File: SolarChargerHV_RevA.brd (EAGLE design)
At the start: 85 x 78 mm, 134 parts, among them CON1 CON_4X200MIL, CON2 USB_BMULTICOMP, CON3 ICSP, CON4 CON_3X100MIL, CON5 CON_3X100MIL, CON6 CON_8X200MIL, CON7 CON_2X100MIL, IC1 MCP3428, IC10 AT45DB161E, IC12 MCP14A0153, IC13 MCP14A0153, IC2 LMR62014, IC3 MIC4605-1YM, IC4 MCP1755, IC5 PIC18F46J50, IC6 TS6001, IC7 LMT86, IC8 24AA16, Q10 NTR4101PT1G, Q11 N-FET, Q12 N-FET, Q13 N-FET, Q14 N-FET, Q15 NX3008NBKW, Q2 PSMN6R0-30YL, Q3 NX3008NBKW, Q4 NTR4101PT1G, Q5 IPB039N10N3, Q6 IPB039N10N3, Q9 NX3008NBKW, X1 ABS07-120-32.768KHZ-T, X2 ABM3-8.000MHZ-D2Y-T, X3 USB_A, X4 USB_A

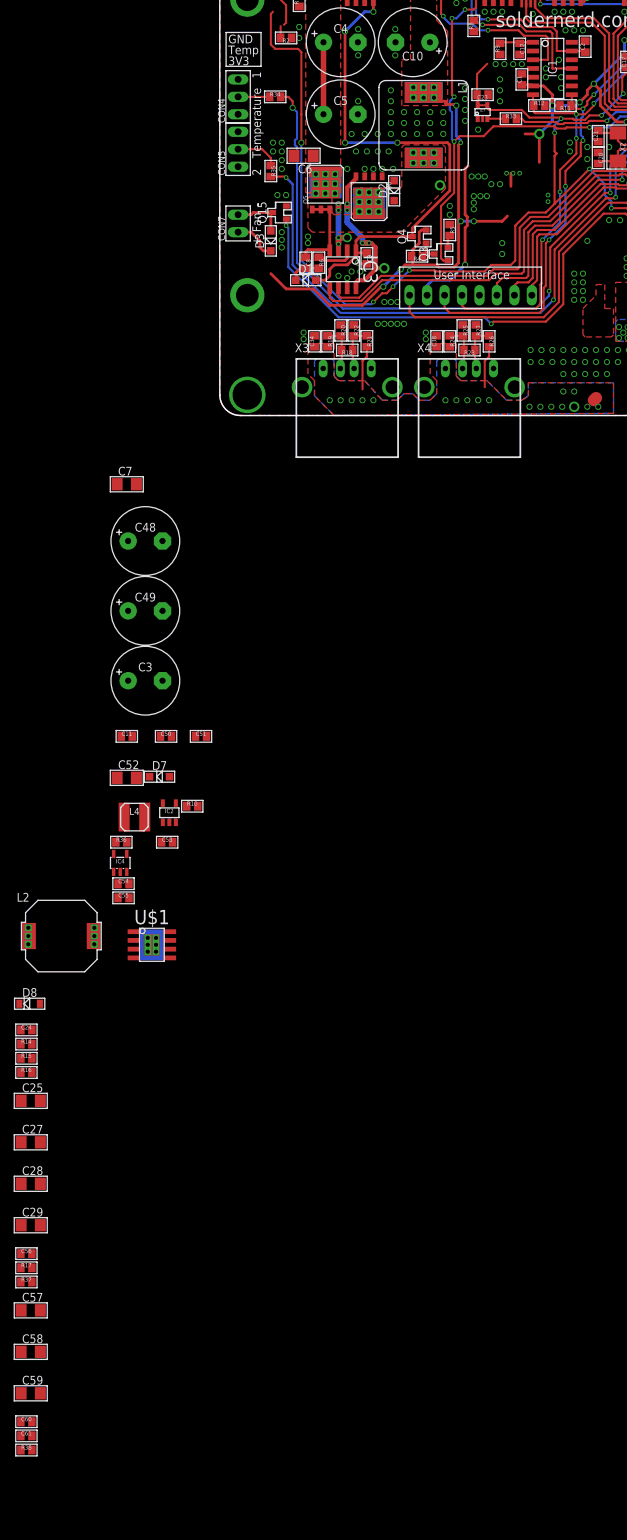
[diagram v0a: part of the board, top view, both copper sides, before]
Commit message: Buck for high voltage version nearly completed. Mosfet footprint still to be changed. Low-side current sensing implemented
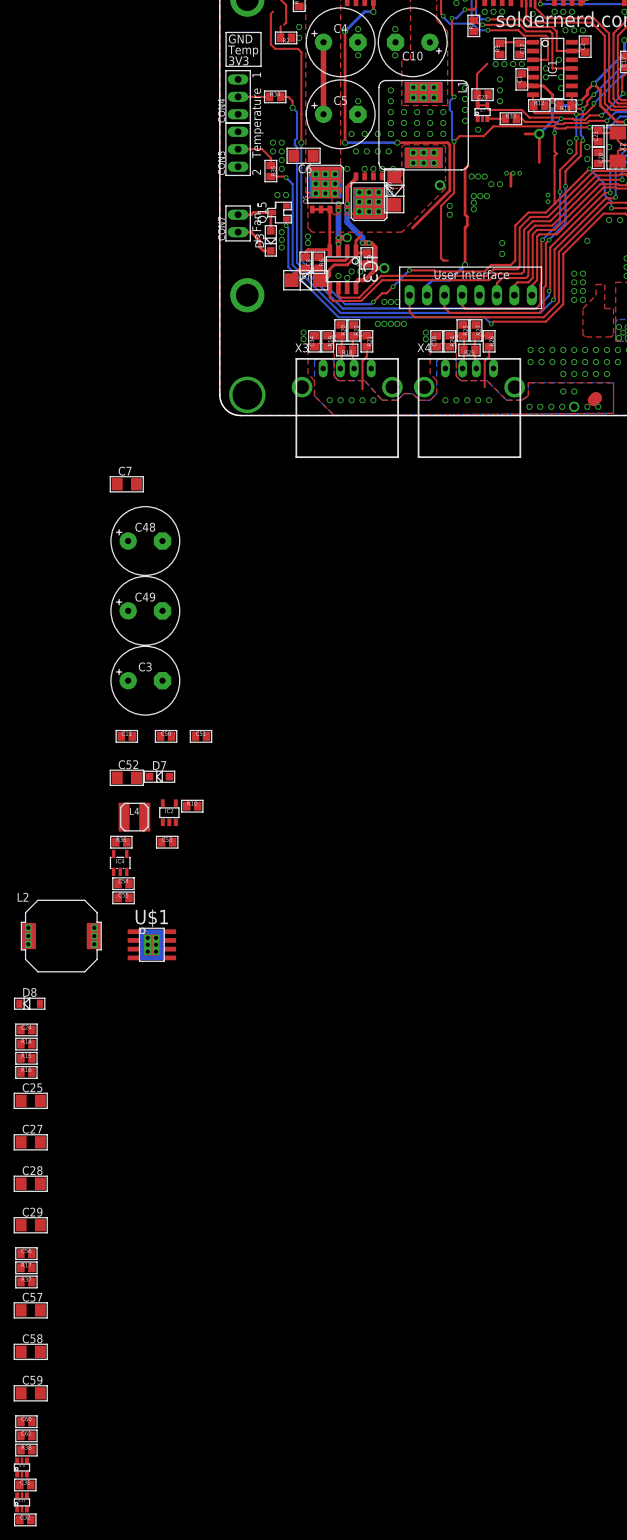
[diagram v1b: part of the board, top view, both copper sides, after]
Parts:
- removed Q3: NX3008NBKW, 00Mosfet:SOT23
- removed Q4: NTR4101PT1G, 00Mosfet:SOT23
- removed R4: 620k, 00Resistor:R0805
- removed R5: 300k, 00Resistor:R0805
- added C31, C32: 100n, 00Capacitor:C0805
- added IC11, IC9: INA213, 00Sensor:SC70-6
- D1, D2: value PMEG3010BER -> STPS2150; device 00Diode:SOD123 -> 00Diode:DO214AC
- D5: value 18V -> 70V
- D6: value 15V -> 48V
- Q2: value PSMN6R0-30YL -> IPB039N10N3
- R3, R7: value R003 -> R0025
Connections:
- removed net N$16: Q3.3, Q4.1, R4.1
- removed net N$19: Q3.2, R5.2
- removed net VIN_SENSE: C2.1, IC1.13, R1.1, R2.2
- removed net VOUT: C10.+, C3.+, L1.1, L1.1B, L1.1C, L1.1D, L1.1E, L1.1F, L1.1G, L1.1H, Q4.2, R4.2
- new net GNDINT: C10.-, C3.-, C4.-, C48.-, C49.-, C5.-, C6.2, C7.2, D2.A, IC11.5, IC9.4, Q6.1, Q6.2, Q6.3, R3.2, R7.1
- new net VIN_SENSE+: C2.2, IC1.13, R1.1, R2.2
- new net VIN_SENSE-: C2.1, IC1.14, IC9.5, Q2.1, Q2.2, Q2.3, R2.1, R3.1
- new net VOUT_SENSE+: C12.1, IC1.1
- net +3V3: now also C31.1, C32.1, IC11.3, IC9.3
- net BATTERY: now also C10.+, C3.+, L1.1, L1.1B, L1.1C, L1.1D, L1.1E, L1.1F, L1.1G, L1.1H
- net BUCK_ON: no longer Q3.1
- net BUCK_SUPPLY: no longer Q4.3
- net GND: now also C31.2, C32.2, IC11.1, IC11.2, IC11.4, IC9.1, IC9.2, R7.2; no longer C10.-, C2.2, C3.-, C4.-, C48.-, C49.-, C5.-, C6.2, C7.2, D2.A, D5.A, IC1.14, Q2.1, Q2.2, Q2.3, Q6.1, Q6.2, Q6.3, R2.1, R5.1
- net IIN_SENSE: now also IC9.6
- net IOUT_SENSE: now also IC11.6
- net PANEL-: now also D5.A
- net VOUT_SENSE: no longer C12.1, IC1.1
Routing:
- net VIN_SENSE: track 84.0 -> 0.00 mm, vias 2 -> 0
- net VIN_SENSE+: track 0.00 -> 83.8 mm, vias 0 -> 2
- net VOUT: track 72.2 -> 0.00 mm, vias 6 -> 0
- net BUCK_SUPPLY: track 74.1 -> 64.6 mm
- net N$16: track 3.43 -> 0.00 mm
- net VOUT_SENSE: track 5.49 -> 3.28 mm
- net N$19: track 1.85 -> 0.00 mm
- net VOUT_SENSE+: track 0.00 -> 1.78 mm
- net N$1: track 4.93 -> 5.52 mm

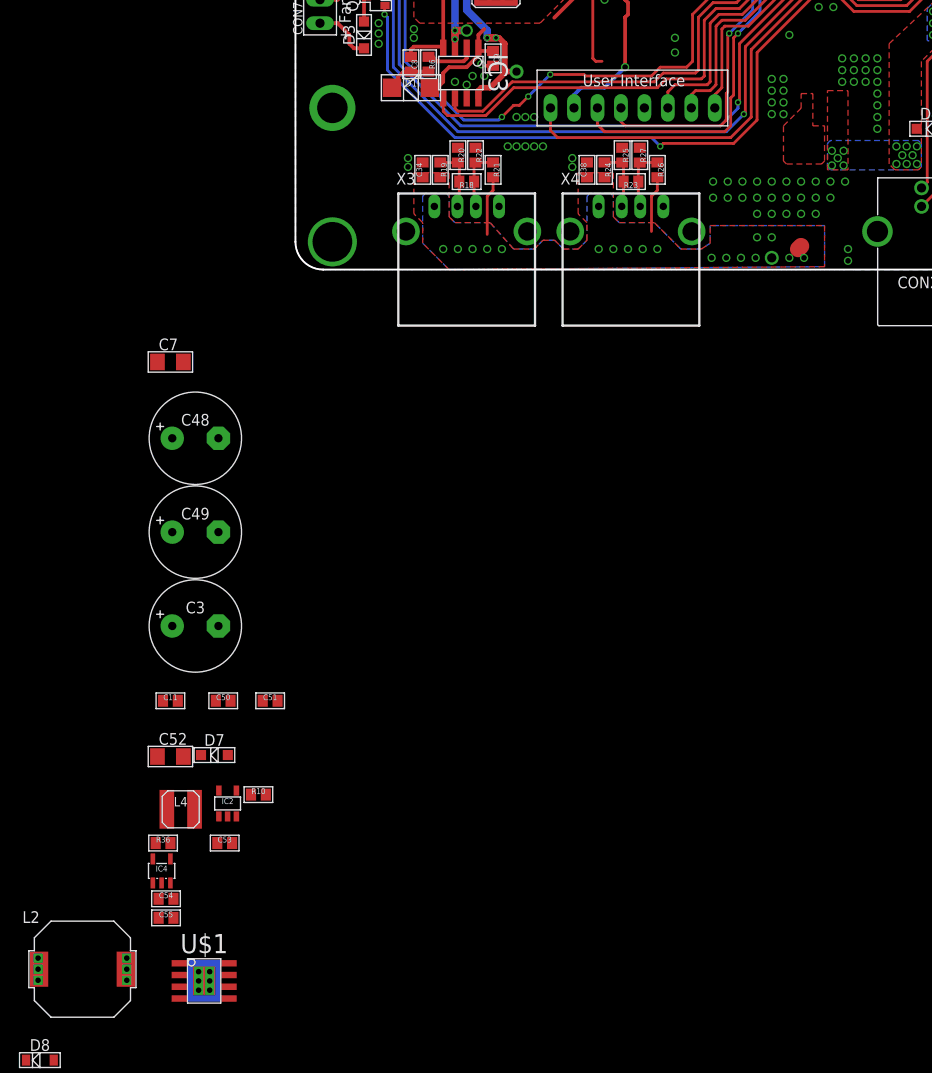
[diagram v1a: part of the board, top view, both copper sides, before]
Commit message: Flash now supplied directly from VCC
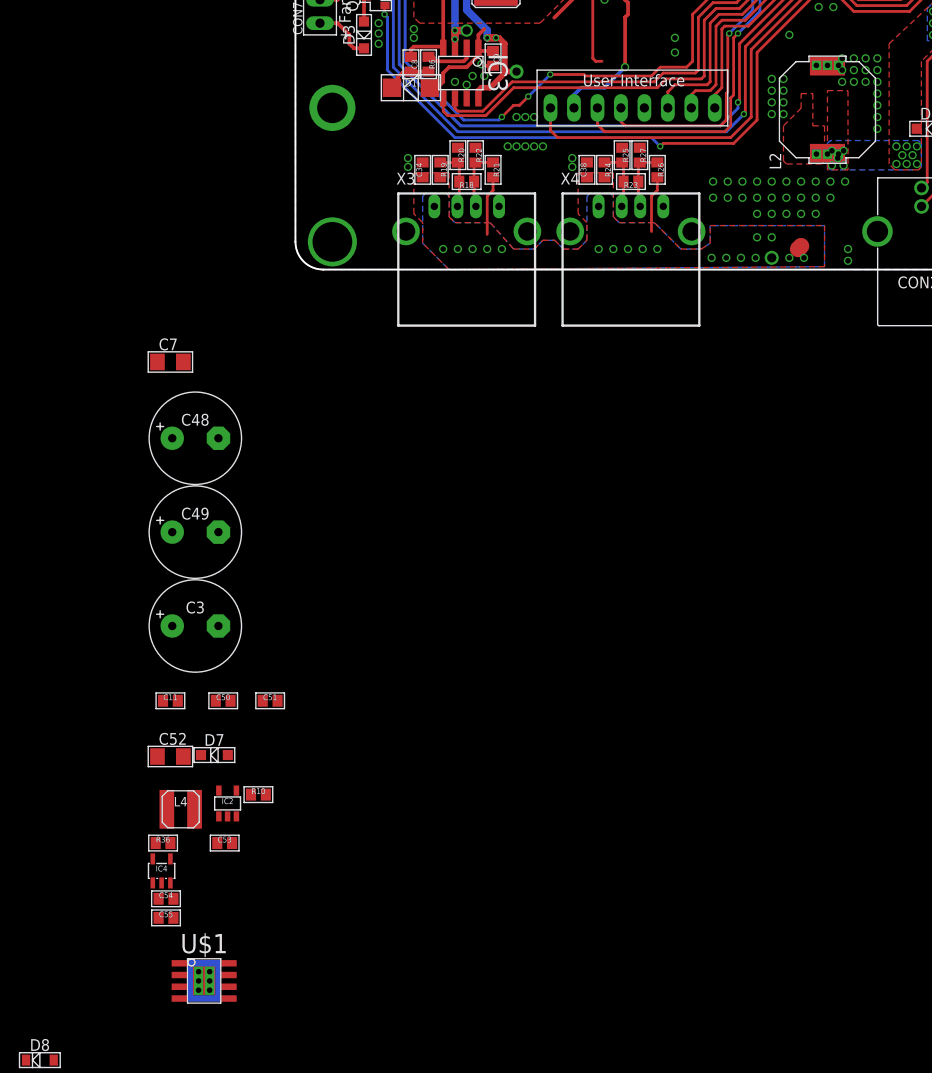
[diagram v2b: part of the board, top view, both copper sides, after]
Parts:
- moved L2 123.1 mm to (65.1, 17.3), turned to 90 degrees
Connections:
- net +3V3: no longer CON4.1, CON5.1
- net +5V: now also CON4.1, CON5.1
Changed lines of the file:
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@@
 <element name="C55" library="00Capacitor" package="C0805" value="10u" x="-6.50875" y="-70.1675"/>
 <element name="U$1" library="00VoltageRegulator" package="SOIC8_PWRPAD" value="TSP54360" x="-2.38125" y="-76.99375"/>
-<element name="L2" library="00Inductor" package="MSS1038" value="8.2u" x="-15.5575" y="-75.72375"/>
+<element name="L2" library="00Inductor" package="MSS1038" value="8.2u" x="65.0875" y="17.30375" rot="R90"/>
 <element name="D8" library="00Diode" package="MINI2-F3-B" value="SCHOTTKYMINI2" x="-20.16125" y="-85.56625"/>
 <element name="C24" library="00Capacitor" package="C0805" value="100n" x="-20.6375" y="-89.37625"/>
@@
 <wire x1="56.99125" y1="43.33875" x2="57.15" y2="43.18" width="0.3048" layer="1"/>
 <wire x1="87.63" y1="27.6225" x2="88.1575" y2="28.15" width="0.3048" layer="1"/>
-<contactref element="CON4" pad="1"/>
 <contactref element="C14" pad="1"/>
 <contactref element="IC5" pad="37"/>
@@
 <wire x1="66.875" y1="50.435" x2="66.675" y2="50.635" width="0.3048" layer="1"/>
 <wire x1="66.8275" y1="50.635" x2="66.675" y2="50.635" width="0.3048" layer="1"/>
-<contactref element="CON5" pad="1"/>
 <contactref element="C31" pad="1"/>
 <contactref element="IC9" pad="3"/>
@@
 <wire x1="82.6575" y1="29.845" x2="81.28" y2="29.845" width="0" layer="19" extent="1-1"/>
 <wire x1="86.995" y1="38.42375" x2="86.995" y2="41.5925" width="0" layer="19" extent="1-1"/>
-<wire x1="10.16" y1="43.815" x2="19.3675" y2="43.815" width="0" layer="19" extent="1-1"/>
-<wire x1="10.16" y1="36.195" x2="10.16" y2="43.815" width="0" layer="19" extent="1-1"/>
 </signal>
 <signal name="LI">
@@
 <wire x1="80.3275" y1="56.045" x2="81.75" y2="56.045" width="0.3048" layer="1"/>
 <wire x1="81.75" y1="56.045" x2="82.2325" y2="55.5625" width="0.3048" layer="1"/>
+<contactref element="CON4" pad="1"/>
+<contactref element="CON5" pad="1"/>
 <wire x1="-21.4375" y1="-123.98375" x2="-21.4375" y2="-121.92" width="0" layer="19" extent="1-1"/>
 <wire x1="-21.4025" y1="-117.7925" x2="-21.4375" y2="-121.92" width="0" layer="19" extent="1-1"/>
@@
 <wire x1="-21.4025" y1="-105.7275" x2="-21.4025" y2="-111.76" width="0" layer="19" extent="1-1"/>
 <wire x1="-21.4025" y1="-99.695" x2="-21.4025" y2="-105.7275" width="0" layer="19" extent="1-1"/>
-<wire x1="-10.7575" y1="-76.92375" x2="-21.4025" y2="-99.695" width="0" layer="19" extent="1-1"/>
-<wire x1="-10.7575" y1="-75.72375" x2="-10.7575" y2="-76.92375" width="0" layer="19" extent="1-1"/>
-<wire x1="-10.8575" y1="-75.72375" x2="-10.7575" y2="-75.72375" width="0" layer="19" extent="16-16"/>
-<wire x1="-10.8575" y1="-75.72375" x2="-10.8575" y2="-75.72375" width="0" layer="19" extent="1-16"/>
-<wire x1="-10.7575" y1="-74.52375" x2="-10.7575" y2="-75.72375" width="0" layer="19" extent="1-1"/>
-<wire x1="-7.30875" y1="-68.10375" x2="-10.7575" y2="-74.52375" width="0" layer="19" extent="1-1"/>
+<wire x1="66.2875" y1="22.10375" x2="-21.4025" y2="-99.695" width="0" layer="19" extent="1-1"/>
+<wire x1="65.0875" y1="22.10375" x2="66.2875" y2="22.10375" width="0" layer="19" extent="1-1"/>
+<wire x1="65.0875" y1="22.00375" x2="65.0875" y2="22.10375" width="0" layer="19" extent="16-16"/>
+<wire x1="65.0875" y1="22.00375" x2="65.0875" y2="22.00375" width="0" layer="19" extent="1-16"/>
+<wire x1="63.8875" y1="22.10375" x2="65.0875" y2="22.10375" width="0" layer="19" extent="1-1"/>
+<wire x1="-7.30875" y1="-68.10375" x2="63.8875" y2="22.10375" width="0" layer="19" extent="1-1"/>
 <wire x1="-7.935" y1="-66.3875" x2="-7.30875" y2="-68.10375" width="0" layer="19" extent="1-1"/>
 <wire x1="-6.035" y1="-66.3875" x2="-7.935" y2="-66.3875" width="0" layer="19" extent="1-1"/>
@@
 <wire x1="57.4675" y1="3.4925" x2="59.055" y2="3.4925" width="0" layer="19" extent="1-1"/>
 <wire x1="14.9225" y1="23.95" x2="21.2725" y2="9.995" width="0" layer="19" extent="1-1"/>
+<wire x1="10.16" y1="36.195" x2="10.16" y2="26.67" width="0" layer="19" extent="1-1"/>
+<wire x1="10.16" y1="43.815" x2="10.16" y2="36.195" width="0" layer="19" extent="1-1"/>
 <wire x1="84.135" y1="53.2925" x2="62.23" y2="2.54" width="0" layer="19" extent="1-1"/>
 </signal>
@@
 <contactref element="D8" pad="C"/>
 <wire x1="-21.66125" y1="-85.56625" x2="-21.4375" y2="-89.37625" width="0" layer="19" extent="1-1"/>
-<wire x1="-20.3575" y1="-76.92375" x2="-21.66125" y2="-85.56625" width="0" layer="19" extent="1-1"/>
-<wire x1="-20.3575" y1="-75.72375" x2="-20.3575" y2="-76.92375" width="0" layer="19" extent="1-1"/>
-<wire x1="-20.2575" y1="-75.72375" x2="-20.3575" y2="-75.72375" width="0" layer="19" extent="16-16"/>
-<wire x1="-20.2575" y1="-75.72375" x2="-20.2575" y2="-75.72375" width="0" layer="19" extent="1-16"/>
-<wire x1="-20.3575" y1="-74.52375" x2="-20.3575" y2="-75.72375" width="0" layer="19" extent="1-1"/>
-<wire x1="0.26875" y1="-75.08875" x2="-20.2575" y2="-75.72375" width="0" layer="19" extent="1-16"/>
+<wire x1="66.2875" y1="12.50375" x2="-21.66125" y2="-85.56625" width="0" layer="19" extent="1-1"/>
+<wire x1="65.0875" y1="12.50375" x2="66.2875" y2="12.50375" width="0" layer="19" extent="1-1"/>
+<wire x1="65.0875" y1="12.60375" x2="65.0875" y2="12.50375" width="0" layer="19" extent="16-16"/>
+<wire x1="65.0875" y1="12.60375" x2="65.0875" y2="12.60375" width="0" layer="19" extent="1-16"/>
+<wire x1="63.8875" y1="12.50375" x2="65.0875" y2="12.50375" width="0" layer="19" extent="1-1"/>
+<wire x1="0.26875" y1="-75.08875" x2="65.0875" y2="12.60375" width="0" layer="19" extent="1-16"/>
 </signal>
 <signal name="N$6">
